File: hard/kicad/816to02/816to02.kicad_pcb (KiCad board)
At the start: 2 copper layers, 4 parts, among them U1 65C02 SOCKET, U2 65C816, U3 74HC245, U4 74HC00

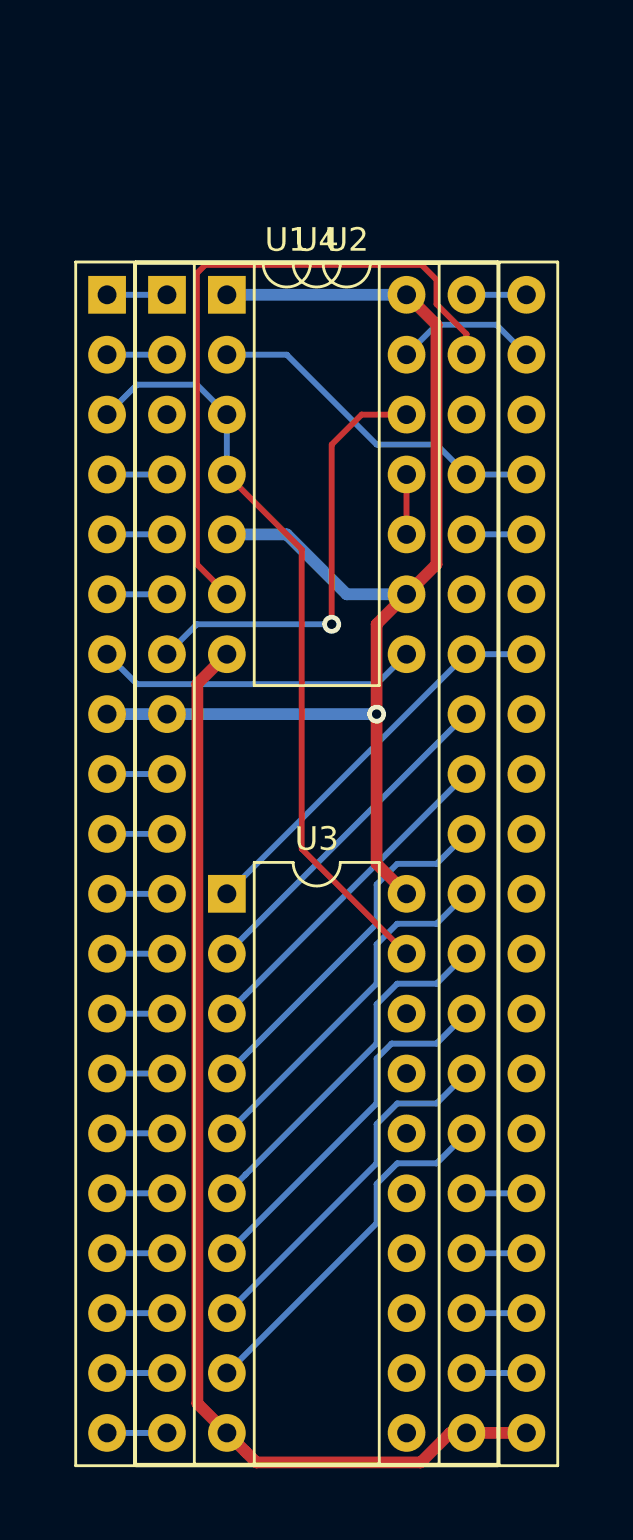
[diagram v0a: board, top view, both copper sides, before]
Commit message: preliminary 65816 adapter
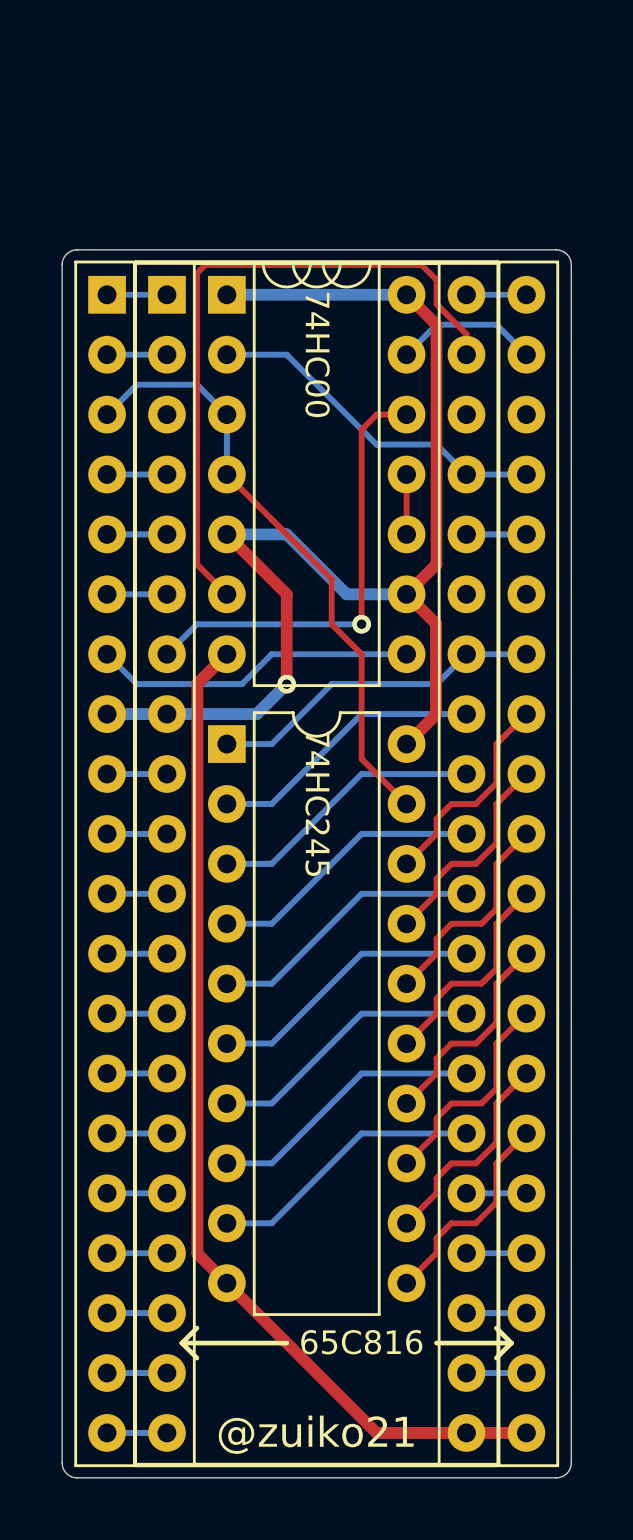
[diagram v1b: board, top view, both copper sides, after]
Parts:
- moved U3 6.35 mm to (23.5, 43.2)
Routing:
- net /BD5: track 0.00 -> 9.20 mm
- net /BD3: track 0.00 -> 9.20 mm
- net /BD2: track 0.00 -> 9.20 mm
- net /BD7: track 0.00 -> 9.06 mm
- net /BD0: track 0.00 -> 9.06 mm
- net /BD1: track 0.00 -> 9.06 mm
- net /BD6: track 0.00 -> 9.06 mm
- net /BD4: track 0.00 -> 9.06 mm
- net /PHI1: track 32.1 -> 27.6 mm
- net GND: track 47.8 -> 43.7 mm
- net /D5: track 15.5 -> 11.7 mm
- net /D6: track 15.3 -> 11.7 mm
- net /D2: track 15.3 -> 11.7 mm
- net /D7: track 15.3 -> 11.7 mm
- net /D4: track 15.3 -> 11.7 mm
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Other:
- board outline added: 21.6 x 52.1 mm
- board text added: "@zuiko21"

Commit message: updates in adapter
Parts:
- added D1: BLUE, LED_THT:LED_D3.0mm_Horizontal_O6.35mm_Z2.0mm, F.Cu at (28.6, 25.4)
- added R1: 12K, Resistor_SMD:R_0805_2012Metric_Pad1.15x1.40mm_HandSolder, F.Cu at (26.0, 29.2)
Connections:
- U2 pad 3: (no net) -> +5V
- U2 pad 35: (no net) -> Net-(R1-Pad1)
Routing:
- net Net-(R1-Pad1): track 0.00 -> 14.5 mm, vias 0 -> 1
- net +5V: track 53.0 -> 62.2 mm
- net Net-(D1-Pad1): track 0.00 -> 4.44 mm
- net /PHI1: track 27.6 -> 28.4 mm, vias 0 -> 1
- added copper zone on B.Cu, net +5V
- added copper zone on F.Cu, net GND
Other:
- board text added: "65C816->65C02 ADAPTER"
- board text added: "K"
- board text added: "v1 2023·06"

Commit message: updated PCBs
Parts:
- added G***: LOGO, durango:j300, F.Cu at (26.8, 71.2)
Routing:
- net +5V: track 62.2 -> 61.4 mm
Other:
- board text added: "JLCJLCJLCJLC"
- board text added: "v1 2023·07"
- board text removed: "v1 2023·06"
